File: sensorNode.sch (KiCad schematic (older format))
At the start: 17 parts, among them P1 PIR, P2 PRGM, P3 Serial I/O, SW1 Reset, U1 ESP-12, U2 DS18B20, U3 ISL29035

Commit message: Placed with 1206 parts
No routing attempted.
Battery is wrong.
Board outline is crude approximation of battery holder

On branch master
new file:   sensorNode.cmp
modified:   sensorNode.kicad_pcb
modified:   sensorNode.sch
new file:   sensorNode.xml
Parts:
- BT1: footprint (none) -> Pin_Headers:Pin_Header_Straight_2x01
- C1: footprint (none) -> Capacitors_SMD:C_1210_HandSoldering
- P1: footprint (none) -> Pin_Headers:Pin_Header_Straight_1x04
- P2: footprint (none) -> Pin_Headers:Pin_Header_Straight_1x02
- P3: footprint (none) -> Pin_Headers:Pin_Header_Straight_1x03
- R1, R2, R3, R4, R5, R6, R7, R8: footprint (none) -> Resistors_SMD:R_1210_HandSoldering
- SW1: footprint (none) -> Buttons_Switches_SMD:SW_SPST_PTS645
- U1: footprint ESP-12_2mm -> ESP8266:ESP-12
- U2: footprint MODULE -> Housings_TO-92:TO-92_Inline_Narrow_Oval
- U3: footprint (none) -> Housings_DFN_QFN:DFN-6-1EP_2x2mm_Pitch0.5mm
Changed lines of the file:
@@
 F 0 "U1" H 5250 5150 50  0000 C CNN
 F 1 "ESP-12" H 4800 4600 50  0000 C CNN
-F 2 "ESP-12_2mm" H 4800 4500 50  0001 C CNN
+F 2 "ESP8266:ESP-12" H 4800 4500 50  0001 C CNN
 F 3 "DOCUMENTATION" H 4800 4500 50  0001 C CNN
 	1    4800 4500
@@
 F 0 "BT1" H 1850 1500 50  0000 L CNN
 F 1 "3v" H 1850 1400 50  0000 L CNN
-F 2 "" V 1750 1490 60  0000 C CNN
+F 2 "Pin_Headers:Pin_Header_Straight_2x01" V 1750 1490 60  0001 C CNN
 F 3 "" V 1750 1490 60  0000 C CNN
 	1    1750 1450
@@
 F 0 "R1" V 2930 3350 50  0000 C CNN
 F 1 "100" V 2850 3350 50  0000 C CNN
-F 2 "" V 2780 3350 30  0000 C CNN
+F 2 "Resistors_SMD:R_1210_HandSoldering" V 2780 3350 30  0001 C CNN
 F 3 "" H 2850 3350 30  0000 C CNN
 	1    2850 3350
@@
 F 0 "R3" V 6180 3800 50  0000 C CNN
 F 1 "10k" V 6100 3800 50  0000 C CNN
-F 2 "" V 6030 3800 30  0000 C CNN
+F 2 "Resistors_SMD:R_1210_HandSoldering" V 6030 3800 30  0001 C CNN
 F 3 "" H 6100 3800 30  0000 C CNN
 	1    6100 3800
@@
 F 0 "R2" V 3330 3350 50  0000 C CNN
 F 1 "10k" V 3250 3350 50  0000 C CNN
-F 2 "" V 3180 3350 30  0000 C CNN
+F 2 "Resistors_SMD:R_1210_HandSoldering" V 3180 3350 30  0001 C CNN
 F 3 "" H 3250 3350 30  0000 C CNN
 	1    3250 3350
@@
 F 0 "C1" H 3275 3950 50  0000 L CNN
 F 1 "C" H 3275 3750 50  0000 L CNN
-F 2 "" H 3288 3700 30  0000 C CNN
+F 2 "Capacitors_SMD:C_1210_HandSoldering" H 3288 3700 30  0001 C CNN
 F 3 "" H 3250 3850 60  0000 C CNN
 	1    3250 3850
@@
 F 0 "R4" V 6180 5200 50  0000 C CNN
 F 1 "1k" V 6100 5200 50  0000 C CNN
-F 2 "" V 6030 5200 30  0000 C CNN
+F 2 "Resistors_SMD:R_1210_HandSoldering" V 6030 5200 30  0001 C CNN
 F 3 "" H 6100 5200 30  0000 C CNN
 	1    6100 5200
@@
 F 0 "SW1" H 3150 5160 50  0000 C CNN
 F 1 "Reset" H 3000 4970 50  0000 C CNN
-F 2 "" H 3000 5050 60  0000 C CNN
+F 2 "Buttons_Switches_SMD:SW_SPST_PTS645" H 3000 5050 60  0001 C CNN
 F 3 "" H 3000 5050 60  0000 C CNN
 	1    3000 5050
@@
 F 0 "P2" H 6800 4800 50  0000 C CNN
 F 1 "PRGM" V 6900 4650 50  0000 C CNN
-F 2 "" H 6800 4650 60  0000 C CNN
+F 2 "Pin_Headers:Pin_Header_Straight_1x02" H 6800 4650 60  0001 C CNN
 F 3 "" H 6800 4650 60  0000 C CNN
 	1    6800 4650
@@
 F 0 "P3" H 7450 4500 50  0000 C CNN
 F 1 "Serial I/O" V 7550 4300 50  0000 C CNN
-F 2 "" H 7450 4300 60  0000 C CNN
+F 2 "Pin_Headers:Pin_Header_Straight_1x03" H 7450 4300 60  0001 C CNN
 F 3 "" H 7450 4300 60  0000 C CNN
 	1    7450 4300
@@
 F 0 "U2" H 8400 5650 50  0000 C CNN
 F 1 "DS18B20" H 8200 5350 50  0000 C CNN
-F 2 "MODULE" H 8450 5000 50  0001 C CNN
+F 2 "Housings_TO-92:TO-92_Inline_Narrow_Oval" H 8450 5000 50  0001 C CNN
 F 3 "DOCUMENTATION" H 7850 5000 50  0001 C CNN
 	1    8200 5300
@@
 F 0 "R8" V 7480 5050 50  0000 C CNN
 F 1 "4.7k" V 7400 5050 50  0000 C CNN
-F 2 "" V 7330 5050 30  0000 C CNN
+F 2 "Resistors_SMD:R_1210_HandSoldering" V 7330 5050 30  0001 C CNN
 F 3 "" H 7400 5050 30  0000 C CNN
 	1    7400 5050
@@
 F 0 "U3" H 8600 3000 50  0000 C CNN
 F 1 "ISL29035" H 8250 2650 50  0000 C CNN
-F 2 "" H 7550 2200 50  0001 C CNN
+F 2 "Housings_DFN_QFN:DFN-6-1EP_2x2mm_Pitch0.5mm" H 7550 2200 50  0001 C CNN
 F 3 "" H 7550 2100 50  0001 C CNN
 	1    8250 2650
@@
 F 0 "P1" V 5150 2450 50  0000 C CNN
 F 1 "PIR" V 5250 2200 50  0000 C CNN
-F 2 "" H 5150 2200 60  0000 C CNN
+F 2 "Pin_Headers:Pin_Header_Straight_1x04" H 5150 2200 60  0001 C CNN
 F 3 "" H 5150 2200 60  0000 C CNN
 	1    5150 2200
@@
 F 0 "R7" V 7330 2200 50  0000 C CNN
 F 1 "4.7k" V 7250 2200 50  0000 C CNN
-F 2 "" V 7180 2200 30  0000 C CNN
+F 2 "Resistors_SMD:R_1210_HandSoldering" V 7180 2200 30  0001 C CNN
 F 3 "" H 7250 2200 30  0000 C CNN
 	1    7250 2200
@@
 F 0 "R6" V 7130 2200 50  0000 C CNN
 F 1 "4.7k" V 7050 2200 50  0000 C CNN
-F 2 "" V 6980 2200 30  0000 C CNN
+F 2 "Resistors_SMD:R_1210_HandSoldering" V 6980 2200 30  0001 C CNN
 F 3 "" H 7050 2200 30  0000 C CNN
 	1    7050 2200
@@
 F 0 "R5" V 6930 2200 50  0000 C CNN
 F 1 "4.7k" V 6850 2200 50  0000 C CNN
-F 2 "" V 6780 2200 30  0000 C CNN
+F 2 "Resistors_SMD:R_1210_HandSoldering" V 6780 2200 30  0001 C CNN
 F 3 "" H 6850 2200 30  0000 C CNN
 	1    6850 2200

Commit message: Multiple changes
- Add bypass cap for isl29035
- Update footprints for battery and isl29035
- place parts on pcb
- possibly others

On branch master
new file:   fp-lib-table
modified:   sensorNode.cmp
modified:   sensorNode.kicad_pcb
modified:   sensorNode.net
modified:   sensorNode.pro
modified:   sensorNode.sch
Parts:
- added C2: 0.1 uF, Capacitors_SMD:C_0603_HandSoldering, symbol C
- BT1: footprint Pin_Headers:Pin_Header_Straight_2x01 -> Battery_Holders:BA2AAPC
- C1: value C -> 0.1 uF; footprint Capacitors_SMD:C_1210_HandSoldering -> Capacitors_SMD:C_0603_HandSoldering
- P1: footprint Pin_Headers:Pin_Header_Straight_1x04 -> Pin_Headers:Pin_Header_Angled_1x04
- P2: footprint Pin_Headers:Pin_Header_Straight_1x02 -> Pin_Headers:Pin_Header_Angled_1x02
- P3: footprint Pin_Headers:Pin_Header_Straight_1x03 -> Pin_Headers:Pin_Header_Angled_1x03
- R1, R2, R3, R4, R5, R6, R7, R8: footprint Resistors_SMD:R_1210_HandSoldering -> Resistors_SMD:R_0603_HandSoldering
- U3: footprint Housings_DFN_QFN:DFN-6-1EP_2x2mm_Pitch0.5mm -> sensorNode:DFN-6_1.5x1.6mm_Pitch0.5mm
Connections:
- net GND: now also C2.2
- net I2C_SCL: no longer R5.2, U1.11 (GPIO2), U3.6 (SDA)
- net VCC: now also C2.1
- new net I2C_SDA: R5.2, U1.11 (GPIO2), U3.6 (SDA)
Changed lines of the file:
@@
 F 0 "BT1" H 1850 1500 50  0000 L CNN
 F 1 "3v" H 1850 1400 50  0000 L CNN
-F 2 "Pin_Headers:Pin_Header_Straight_2x01" V 1750 1490 60  0001 C CNN
+F 2 "Battery_Holders:BA2AAPC" V 1750 1490 60  0001 C CNN
 F 3 "" V 1750 1490 60  0000 C CNN
 	1    1750 1450
@@
 F 0 "R1" V 2930 3350 50  0000 C CNN
 F 1 "100" V 2850 3350 50  0000 C CNN
-F 2 "Resistors_SMD:R_1210_HandSoldering" V 2780 3350 30  0001 C CNN
+F 2 "Resistors_SMD:R_0603_HandSoldering" V 2780 3350 30  0001 C CNN
 F 3 "" H 2850 3350 30  0000 C CNN
 	1    2850 3350
@@
 F 0 "R3" V 6180 3800 50  0000 C CNN
 F 1 "10k" V 6100 3800 50  0000 C CNN
-F 2 "Resistors_SMD:R_1210_HandSoldering" V 6030 3800 30  0001 C CNN
+F 2 "Resistors_SMD:R_0603_HandSoldering" V 6030 3800 30  0001 C CNN
 F 3 "" H 6100 3800 30  0000 C CNN
 	1    6100 3800
@@
 F 0 "R2" V 3330 3350 50  0000 C CNN
 F 1 "10k" V 3250 3350 50  0000 C CNN
-F 2 "Resistors_SMD:R_1210_HandSoldering" V 3180 3350 30  0001 C CNN
+F 2 "Resistors_SMD:R_0603_HandSoldering" V 3180 3350 30  0001 C CNN
 F 3 "" H 3250 3350 30  0000 C CNN
 	1    3250 3350
@@
 P 3250 3850
 F 0 "C1" H 3275 3950 50  0000 L CNN
-F 1 "C" H 3275 3750 50  0000 L CNN
-F 2 "Capacitors_SMD:C_1210_HandSoldering" H 3288 3700 30  0001 C CNN
+F 1 "0.1 uF" H 3275 3750 50  0000 L CNN
+F 2 "Capacitors_SMD:C_0603_HandSoldering" H 3288 3700 30  0001 C CNN
 F 3 "" H 3250 3850 60  0000 C CNN
 	1    3250 3850
@@
 F 0 "R4" V 6180 5200 50  0000 C CNN
 F 1 "1k" V 6100 5200 50  0000 C CNN
-F 2 "Resistors_SMD:R_1210_HandSoldering" V 6030 5200 30  0001 C CNN
+F 2 "Resistors_SMD:R_0603_HandSoldering" V 6030 5200 30  0001 C CNN
 F 3 "" H 6100 5200 30  0000 C CNN
 	1    6100 5200
@@
 F 0 "P2" H 6800 4800 50  0000 C CNN
 F 1 "PRGM" V 6900 4650 50  0000 C CNN
-F 2 "Pin_Headers:Pin_Header_Straight_1x02" H 6800 4650 60  0001 C CNN
+F 2 "Pin_Headers:Pin_Header_Angled_1x02" H 6800 4650 60  0001 C CNN
 F 3 "" H 6800 4650 60  0000 C CNN
 	1    6800 4650
@@
 F 0 "P3" H 7450 4500 50  0000 C CNN
 F 1 "Serial I/O" V 7550 4300 50  0000 C CNN
-F 2 "Pin_Headers:Pin_Header_Straight_1x03" H 7450 4300 60  0001 C CNN
+F 2 "Pin_Headers:Pin_Header_Angled_1x03" H 7450 4300 60  0001 C CNN
 F 3 "" H 7450 4300 60  0000 C CNN
 	1    7450 4300
@@
 F 0 "R8" V 7480 5050 50  0000 C CNN
 F 1 "4.7k" V 7400 5050 50  0000 C CNN
-F 2 "Resistors_SMD:R_1210_HandSoldering" V 7330 5050 30  0001 C CNN
+F 2 "Resistors_SMD:R_0603_HandSoldering" V 7330 5050 30  0001 C CNN
 F 3 "" H 7400 5050 30  0000 C CNN
 	1    7400 5050
@@
 F 0 "U3" H 8600 3000 50  0000 C CNN
 F 1 "ISL29035" H 8250 2650 50  0000 C CNN
-F 2 "Housings_DFN_QFN:DFN-6-1EP_2x2mm_Pitch0.5mm" H 7550 2200 50  0001 C CNN
+F 2 "sensorNode:DFN-6_1.5x1.6mm_Pitch0.5mm" H 7550 2200 50  0001 C CNN
 F 3 "" H 7550 2100 50  0001 C CNN
 	1    8250 2650
@@
 F 0 "P1" V 5150 2450 50  0000 C CNN
 F 1 "PIR" V 5250 2200 50  0000 C CNN
-F 2 "Pin_Headers:Pin_Header_Straight_1x04" H 5150 2200 60  0001 C CNN
+F 2 "Pin_Headers:Pin_Header_Angled_1x04" H 5150 2200 60  0001 C CNN
 F 3 "" H 5150 2200 60  0000 C CNN
 	1    5150 2200
@@
 F 0 "R7" V 7330 2200 50  0000 C CNN
 F 1 "4.7k" V 7250 2200 50  0000 C CNN
-F 2 "Resistors_SMD:R_1210_HandSoldering" V 7180 2200 30  0001 C CNN
+F 2 "Resistors_SMD:R_0603_HandSoldering" V 7180 2200 30  0001 C CNN
 F 3 "" H 7250 2200 30  0000 C CNN
 	1    7250 2200
@@
 F 0 "R6" V 7130 2200 50  0000 C CNN
 F 1 "4.7k" V 7050 2200 50  0000 C CNN
-F 2 "Resistors_SMD:R_1210_HandSoldering" V 6980 2200 30  0001 C CNN
+F 2 "Resistors_SMD:R_0603_HandSoldering" V 6980 2200 30  0001 C CNN
 F 3 "" H 7050 2200 30  0000 C CNN
 	1    7050 2200
@@
 F 0 "R5" V 6930 2200 50  0000 C CNN
 F 1 "4.7k" V 6850 2200 50  0000 C CNN
-F 2 "Resistors_SMD:R_1210_HandSoldering" V 6780 2200 30  0001 C CNN
+F 2 "Resistors_SMD:R_0603_HandSoldering" V 6780 2200 30  0001 C CNN
 F 3 "" H 6850 2200 30  0000 C CNN
 	1    6850 2200
@@
 	7050 2350 7050 2650
 Wire Wire Line
-	2400 2650 7450 2650
-Wire Wire Line
 	6850 2350 6850 2550
 Wire Wire Line
-	6400 2550 7450 2550
-Wire Wire Line
 	6850 2050 6850 1950
 Wire Wire Line
-	6850 1950 8250 1950
+	6850 1950 8950 1950
 Connection ~ 8250 1950
 Wire Wire Line
@@
 I2C_SDA
 Connection ~ 6850 2550
-Text Label 6400 2550 0    60   ~ 0
-I2C_SDA
 Connection ~ 7050 2650
-Text Label 6400 2650 0    60   ~ 0
-I2C_SCL
 Wire Wire Line
 	2400 4600 3900 4600
@@
 Wire Wire Line
 	8200 4500 8200 4700
+Wire Wire Line
+	6400 2550 7450 2550
+Wire Wire Line
+	2400 2650 7450 2650
+$Comp
+L C C2
+U 1 1 55612960
+P 8950 2100
+F 0 "C2" H 8975 2200 50  0000 L CNN
+F 1 "0.1 uF" H 8975 2000 50  0000 L CNN
+F 2 "Capacitors_SMD:C_0603_HandSoldering" H 8988 1950 30  0001 C CNN
+F 3 "" H 8950 2100 60  0000 C CNN
+	1    8950 2100
+	1    0    0    -1
+$EndComp
+$Comp
+L GND #PWR018
+U 1 1 55612B3E
+P 8950 2350
+F 0 "#PWR018" H 8950 2100 50  0001 C CNN
+F 1 "GND" H 8950 2200 50  0000 C CNN
+F 2 "" H 8950 2350 60  0000 C CNN
+F 3 "" H 8950 2350 60  0000 C CNN
+	1    8950 2350
+	1    0    0    -1
+$EndComp
+Wire Wire Line
+	8950 2350 8950 2250
 $EndSCHEMATC

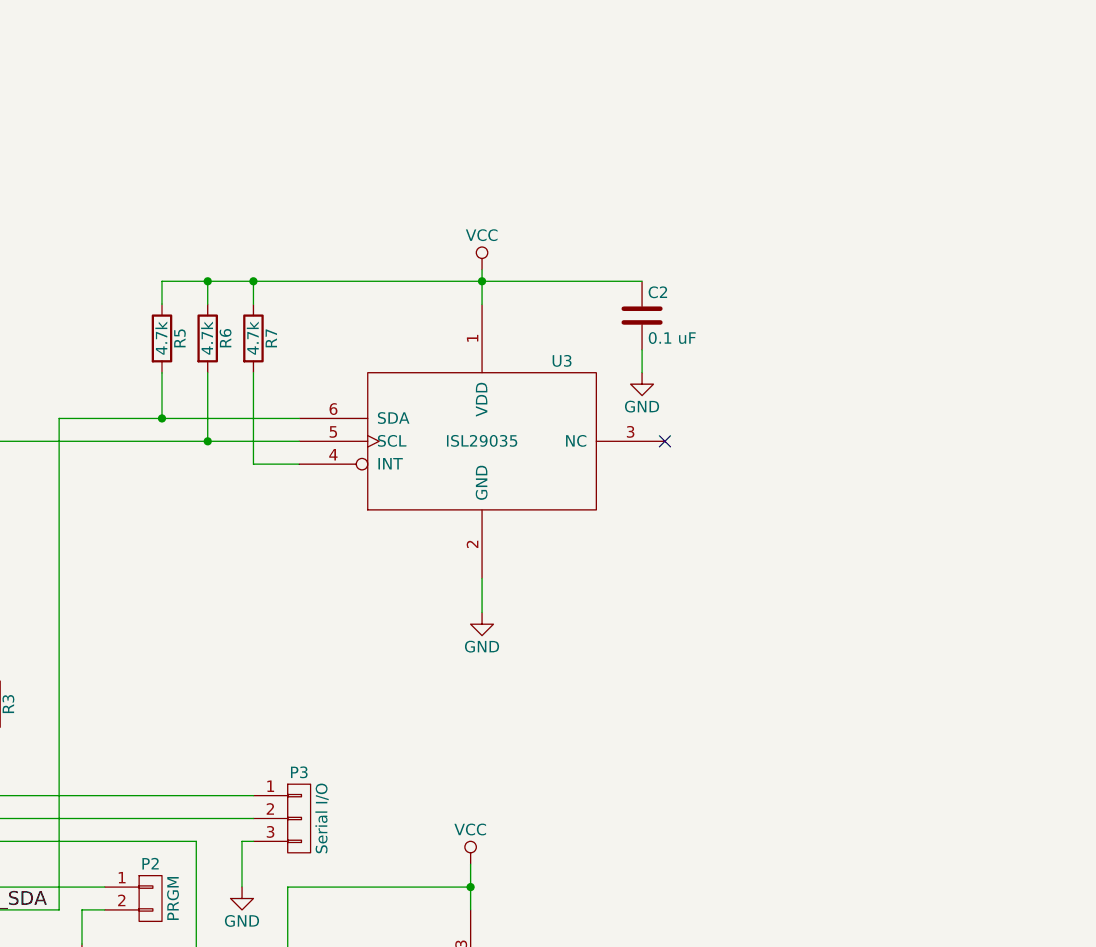
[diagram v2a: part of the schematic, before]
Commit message: Add net-tie to divide pwr nets for routing
On branch newPCB
modified:   sensorNode-cache.lib
new file:   sensorNode.net
modified:   sensorNode.pro
modified:   sensorNode.sch
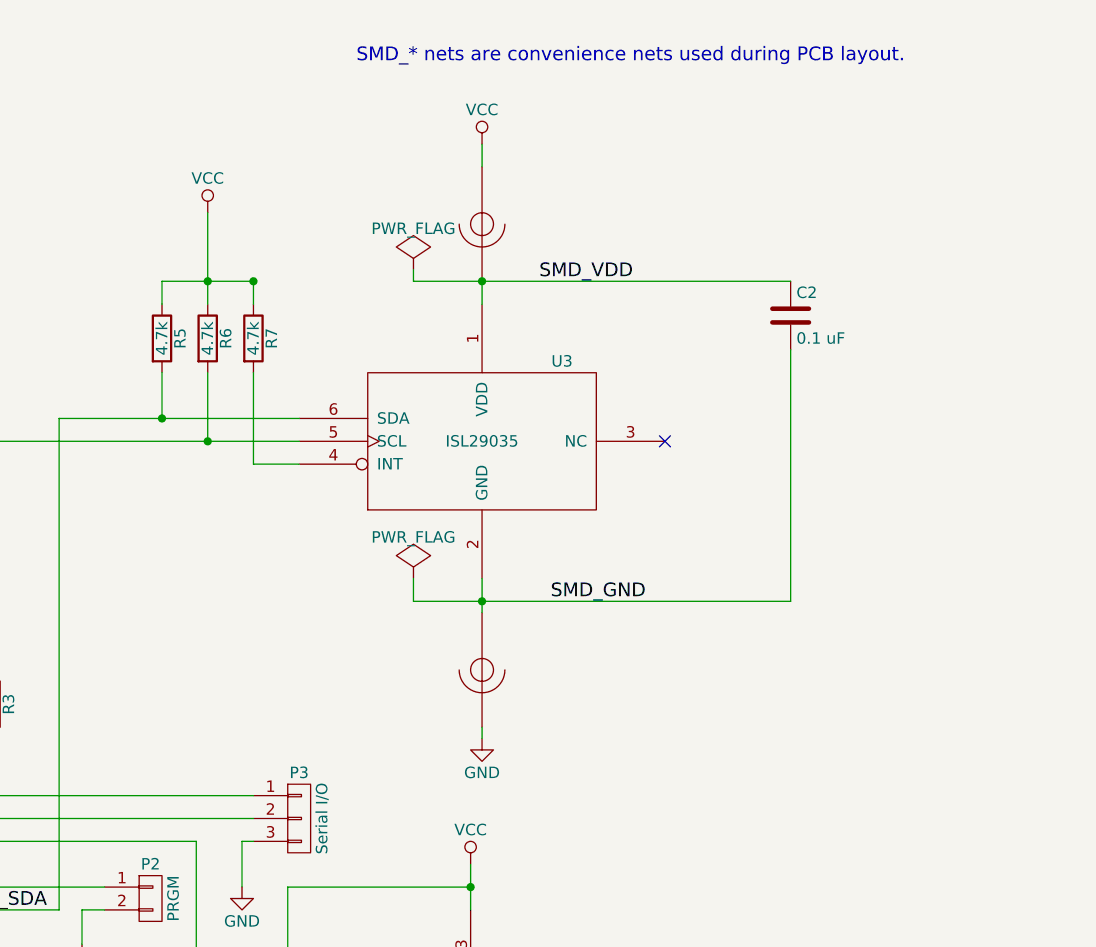
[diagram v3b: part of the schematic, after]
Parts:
- added NT1, NT2: Net-Tie-2, symbol Net-Tie-2
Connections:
- net GND: now also NT2.2; no longer C2.2, U3.2 (GND)
- net VCC: now also NT1.1; no longer C2.1, U3.1 (VDD)
- new net SMD_GND: C2.2, NT2.1, U3.2 (GND)
- new net SMD_VDD: C2.1, NT1.2, U3.1 (VDD)
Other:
- note added: "SMD_* nets are convenience nets used during PCB layout."
- moved on the sheet: C2
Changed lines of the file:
@@
 LIBS:ISL29035
 LIBS:DS7505
+LIBS:net-tie
 LIBS:sensorNode-cache
 EELAYER 25 0
@@
 Wire Wire Line
 	4850 2350 4950 2350
-$Comp
-L GND #PWR016
-U 1 1 5558FF32
-P 8250 3400
-F 0 "#PWR016" H 8250 3150 50  0001 C CNN
-F 1 "GND" H 8250 3250 50  0000 C CNN
-F 2 "" H 8250 3400 60  0000 C CNN
-F 3 "" H 8250 3400 60  0000 C CNN
-	1    8250 3400
-	1    0    0    -1
-$EndComp
-$Comp
-L VCC #PWR017
-U 1 1 5558FF59
-P 8250 1900
-F 0 "#PWR017" H 8250 1750 50  0001 C CNN
-F 1 "VCC" H 8250 2050 50  0000 C CNN
-F 2 "" H 8250 1900 60  0000 C CNN
-F 3 "" H 8250 1900 60  0000 C CNN
-	1    8250 1900
-	1    0    0    -1
-$EndComp
-Wire Wire Line
-	8250 1900 8250 2050
-Wire Wire Line
-	8250 3400 8250 3250
 NoConn ~ 9050 2650
 $Comp
@@
 Wire Wire Line
 	6850 2050 6850 1950
-Wire Wire Line
-	6850 1950 8950 1950
 Connection ~ 8250 1950
 Wire Wire Line
-	7050 2050 7050 1950
+	7050 1650 7050 2050
 Connection ~ 7050 1950
 Wire Wire Line
-	7250 2050 7250 1950
+	7250 1950 7250 2050
 Connection ~ 7250 1950
 Wire Wire Line
@@
 L C C2
 U 1 1 55612960
-P 8950 2100
-F 0 "C2" H 8975 2200 50  0000 L CNN
-F 1 "0.1 uF" H 8975 2000 50  0000 L CNN
-F 2 "Capacitors_SMD:C_0603_HandSoldering" H 8988 1950 30  0001 C CNN
-F 3 "" H 8950 2100 60  0000 C CNN
-	1    8950 2100
-	1    0    0    -1
-$EndComp
-$Comp
-L GND #PWR018
-U 1 1 55612B3E
-P 8950 2350
-F 0 "#PWR018" H 8950 2100 50  0001 C CNN
-F 1 "GND" H 8950 2200 50  0000 C CNN
-F 2 "" H 8950 2350 60  0000 C CNN
-F 3 "" H 8950 2350 60  0000 C CNN
-	1    8950 2350
-	1    0    0    -1
-$EndComp
-Wire Wire Line
-	8950 2350 8950 2250
+P 9600 2100
+F 0 "C2" H 9625 2200 50  0000 L CNN
+F 1 "0.1 uF" H 9625 2000 50  0000 L CNN
+F 2 "Capacitors_SMD:C_0603_HandSoldering" H 9638 1950 30  0001 C CNN
+F 3 "" H 9600 2100 60  0000 C CNN
+	1    9600 2100
+	1    0    0    -1
+$EndComp
+Wire Wire Line
+	9600 3350 9600 2250
+Wire Wire Line
+	7950 3350 9600 3350
+Connection ~ 8250 3350
+$Comp
+L VCC #PWR016
+U 1 1 556A2D43
+P 7050 1650
+F 0 "#PWR016" H 7050 1500 50  0001 C CNN
+F 1 "VCC" H 7050 1800 50  0000 C CNN
+F 2 "" H 7050 1650 60  0000 C CNN
+F 3 "" H 7050 1650 60  0000 C CNN
+	1    7050 1650
+	1    0    0    -1
+$EndComp
+Wire Wire Line
+	6850 1950 7250 1950
+Wire Wire Line
+	7950 1950 9600 1950
+$Comp
+L GND #PWR017
+U 1 1 556A4E30
+P 8250 3950
+F 0 "#PWR017" H 8250 3700 50  0001 C CNN
+F 1 "GND" H 8250 3800 50  0000 C CNN
+F 2 "" H 8250 3950 60  0000 C CNN
+F 3 "" H 8250 3950 60  0000 C CNN
+	1    8250 3950
+	1    0    0    -1
+$EndComp
+$Comp
+L VCC #PWR018
+U 1 1 556A5084
+P 8250 1350
+F 0 "#PWR018" H 8250 1200 50  0001 C CNN
+F 1 "VCC" H 8250 1500 50  0000 C CNN
+F 2 "" H 8250 1350 60  0000 C CNN
+F 3 "" H 8250 1350 60  0000 C CNN
+	1    8250 1350
+	1    0    0    -1
+$EndComp
+Text Label 8500 1950 0    60   ~ 0
+SMD_VDD
+$Comp
+L Net-Tie-2 NT1
+U 1 1 556A552C
+P 8250 1700
+F 0 "NT1" H 8200 1550 60  0001 C CNN
+F 1 "Net-Tie-2" H 8200 1800 60  0001 C CNN
+F 2 "" H 8250 1700 60  0000 C CNN
+F 3 "" H 8250 1700 60  0000 C CNN
+	1    8250 1700
+	0    1    1    0
+$EndComp
+$Comp
+L Net-Tie-2 NT2
+U 1 1 556A55D0
+P 8250 3650
+F 0 "NT2" H 8200 3500 60  0001 C CNN
+F 1 "Net-Tie-2" H 8200 3750 60  0001 C CNN
+F 2 "" H 8250 3650 60  0000 C CNN
+F 3 "" H 8250 3650 60  0000 C CNN
+	1    8250 3650
+	0    1    1    0
+$EndComp
+Wire Wire Line
+	8250 3250 8250 3400
+Wire Wire Line
+	8250 3900 8250 3950
+Wire Wire Line
+	8250 1950 8250 2050
+Wire Wire Line
+	8250 1350 8250 1450
+$Comp
+L PWR_FLAG #FLG019
+U 1 1 556A5A90
+P 7950 1900
+F 0 "#FLG019" H 7950 1995 50  0001 C CNN
+F 1 "PWR_FLAG" H 7950 2080 50  0000 C CNN
+F 2 "" H 7950 1900 60  0000 C CNN
+F 3 "" H 7950 1900 60  0000 C CNN
+	1    7950 1900
+	1    0    0    -1
+$EndComp
+$Comp
+L PWR_FLAG #FLG020
+U 1 1 556A5ADA
+P 7950 3250
+F 0 "#FLG020" H 7950 3345 50  0001 C CNN
+F 1 "PWR_FLAG" H 7950 3430 50  0000 C CNN
+F 2 "" H 7950 3250 60  0000 C CNN
+F 3 "" H 7950 3250 60  0000 C CNN
+	1    7950 3250
+	1    0    0    -1
+$EndComp
+Wire Wire Line
+	7950 1900 7950 1950
+Wire Wire Line
+	7950 3250 7950 3350
+Text Label 8550 3350 0    60   ~ 0
+SMD_GND
+Text Notes 7700 1000 0    60   ~ 0
+SMD_* nets are convenience nets used during PCB layout.
 $EndSCHEMATC

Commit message: Check-point: components placed
Schematic was modified to swap signals on connector pins
to make routing easier.

On branch newPCB
modified:   rockingdlabs_letter_with_logo.kicad_wks
modified:   sensorNode.cmp
new file:   sensorNode.kicad_pcb
modified:   sensorNode.net
modified:   sensorNode.sch
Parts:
- NT1, NT2: footprint (none) -> Oddities:NetTie-I_Connected_SMD
- SW1: footprint Buttons_Switches_SMD:SW_SPST_PTS645 -> Buttons_Switches_SMD:SW_SPST_E-Switch_TL3302BF180QG
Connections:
- net PIR-Motion: now also P1.3 (P3); no longer P1.2 (P2)
- net PIR-Repeat: now also P1.2 (P2); no longer P1.3 (P3)
- net at U1.15 (RXD): now also P3.1 (P1); no longer P3.2 (P2)
- net at U1.16 (TXD): now also P3.2 (P2); no longer P3.1 (P1)
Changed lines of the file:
@@
 F 0 "SW1" H 3150 5160 50  0000 C CNN
 F 1 "Reset" H 3000 4970 50  0000 C CNN
-F 2 "Buttons_Switches_SMD:SW_SPST_PTS645" H 3000 5050 60  0001 C CNN
+F 2 "Buttons_Switches_SMD:SW_SPST_E-Switch_TL3302BF180QG" H 3000 5050 60  0001 C CNN
 F 3 "" H 3000 5050 60  0000 C CNN
 	1    3000 5050
@@
 Connection ~ 6100 4600
 Connection ~ 6100 5500
-Wire Wire Line
-	7250 4200 5700 4200
-Wire Wire Line
-	7250 4300 5700 4300
 $Comp
 L GND #PWR010
@@
 $EndComp
 Wire Wire Line
-	2650 2250 4950 2250
+	2650 2250 4650 2250
 $Comp
 L GND #PWR014
@@
 NoConn ~ 5700 4500
 NoConn ~ 3900 4300
-Text Label 4300 2250 0    60   ~ 0
+Text Label 3100 2250 0    60   ~ 0
 PIR-Repeat
 Wire Wire Line
-	2550 2150 4950 2150
+	2550 2150 4500 2150
 Wire Wire Line
 	2650 2250 2650 4700
 Wire Wire Line
 	2550 2150 2550 4800
-Text Label 4100 2150 0    60   ~ 0
+Text Label 3250 2150 0    60   ~ 0
 PIR-Motion
 Wire Wire Line
@@
 F 0 "NT1" H 8200 1550 60  0001 C CNN
 F 1 "Net-Tie-2" H 8200 1800 60  0001 C CNN
-F 2 "" H 8250 1700 60  0000 C CNN
+F 2 "Oddities:NetTie-I_Connected_SMD" H 8250 1700 60  0001 C CNN
 F 3 "" H 8250 1700 60  0000 C CNN
 	1    8250 1700
@@
 F 0 "NT2" H 8200 3500 60  0001 C CNN
 F 1 "Net-Tie-2" H 8200 3750 60  0001 C CNN
-F 2 "" H 8250 3650 60  0000 C CNN
+F 2 "Oddities:NetTie-I_Connected_SMD" H 8250 3650 60  0001 C CNN
 F 3 "" H 8250 3650 60  0000 C CNN
 	1    8250 3650
@@
 Text Notes 7700 1000 0    60   ~ 0
 SMD_* nets are convenience nets used during PCB layout.
+Wire Wire Line
+	5700 4200 6550 4200
+Wire Wire Line
+	6550 4200 6550 4300
+Wire Wire Line
+	6550 4300 7250 4300
+Wire Wire Line
+	5700 4300 6450 4300
+Wire Wire Line
+	6450 4300 6450 4250
+Wire Wire Line
+	6450 4250 6650 4250
+Wire Wire Line
+	6650 4250 6650 4200
+Wire Wire Line
+	6650 4200 7250 4200
+Wire Wire Line
+	4950 2150 4650 2150
+Wire Wire Line
+	4650 2150 4650 2250
+Wire Wire Line
+	4500 2150 4500 2200
+Wire Wire Line
+	4500 2200 4750 2200
+Wire Wire Line
+	4750 2200 4750 2250
+Wire Wire Line
+	4750 2250 4950 2250
 $EndSCHEMATC
